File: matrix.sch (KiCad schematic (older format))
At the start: 180 parts

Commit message: Matrix work
Additional work on the switch matrix.
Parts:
- removed D? (x3): SOD-123, Diode_SMD:D_SOD-123, symbol Device:D_Small
- removed SW-M? (x2): MX_Alps-1U, MX_Alps_Hybrid:MX-1U-NoLED, symbol MX_Alps_Hybrid:MX-NoLED
- added SW-ISOEN1: MX_Alps-ISO, MX_Alps_Hybrid:MX-ISO-ReversedStabilizers, symbol MX_Alps_Hybrid:MX-NoLED
- added SW-LSHFT2: MX_Alps-1.25U, MX_Alps_Hybrid:MX-1.25U-NoLED, symbol MX_Alps_Hybrid:MX-NoLED
- added SW-STEPCAPS1: MX_Alps-1.75U, MX_Alps_Hybrid:MX-1.75U-NoLED, symbol MX_Alps_Hybrid:MX-NoLED
- SW-ANSIEN1: renamed from SW-M?; value MX_Alps-1U -> MX_Alps-2.25U; footprint MX_Alps_Hybrid:MX-1U-NoLED -> MX_Alps_Hybrid:MX-2.25U-NoLED
- SW-CAPS1, SW-RSHFT1: renamed from SW-M?; value MX_Alps-1U -> MX_Alps-1.75U; footprint MX_Alps_Hybrid:MX-1U-NoLED -> MX_Alps_Hybrid:MX-1.75U-NoLED
- SW-LSHFT1: renamed from SW-M?; footprint MX_Alps_Hybrid:MX-1U-NoLED -> MX_Alps_Hybrid:MX-2.25U-NoLED
- gave numbers to parts that had none: 42
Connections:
- wire segments 159 -> 248
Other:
- moved on the sheet: D1, D10, D11, D12, D13, D14, D15, D16, D17, D18, D19, D2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

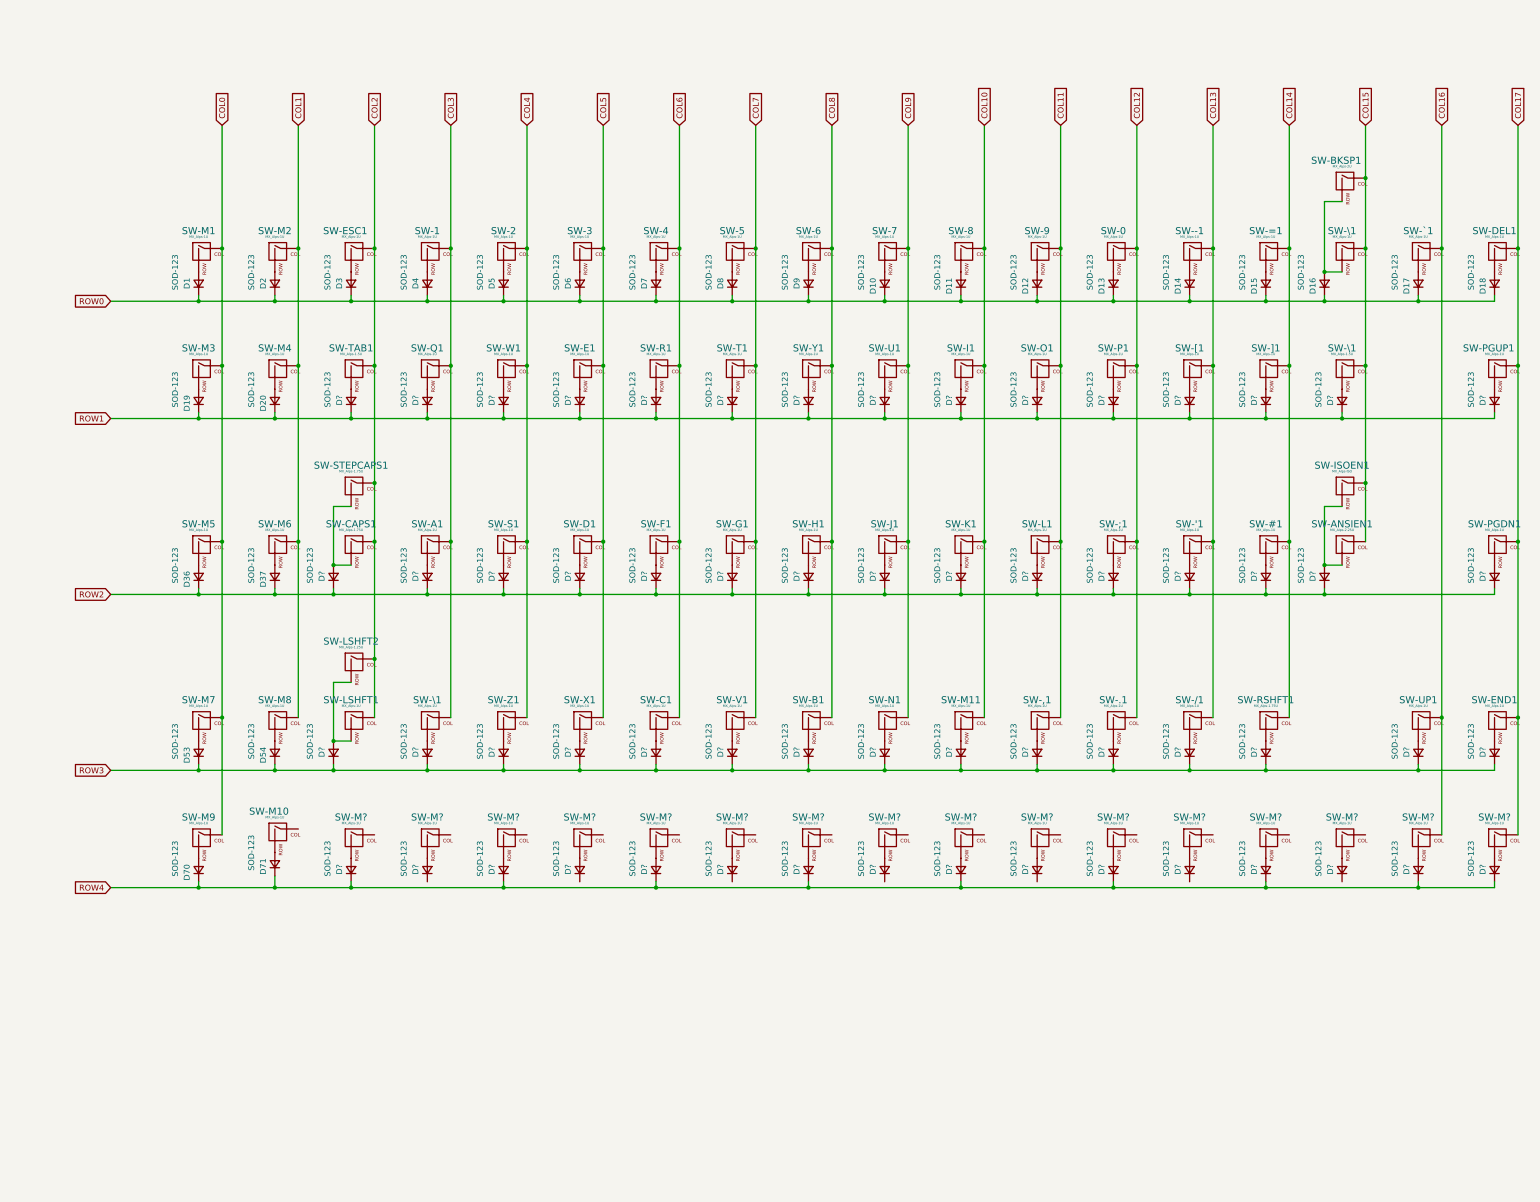
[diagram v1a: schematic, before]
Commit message: Matrix Draft complete
First draft of the switch matrix is complete.
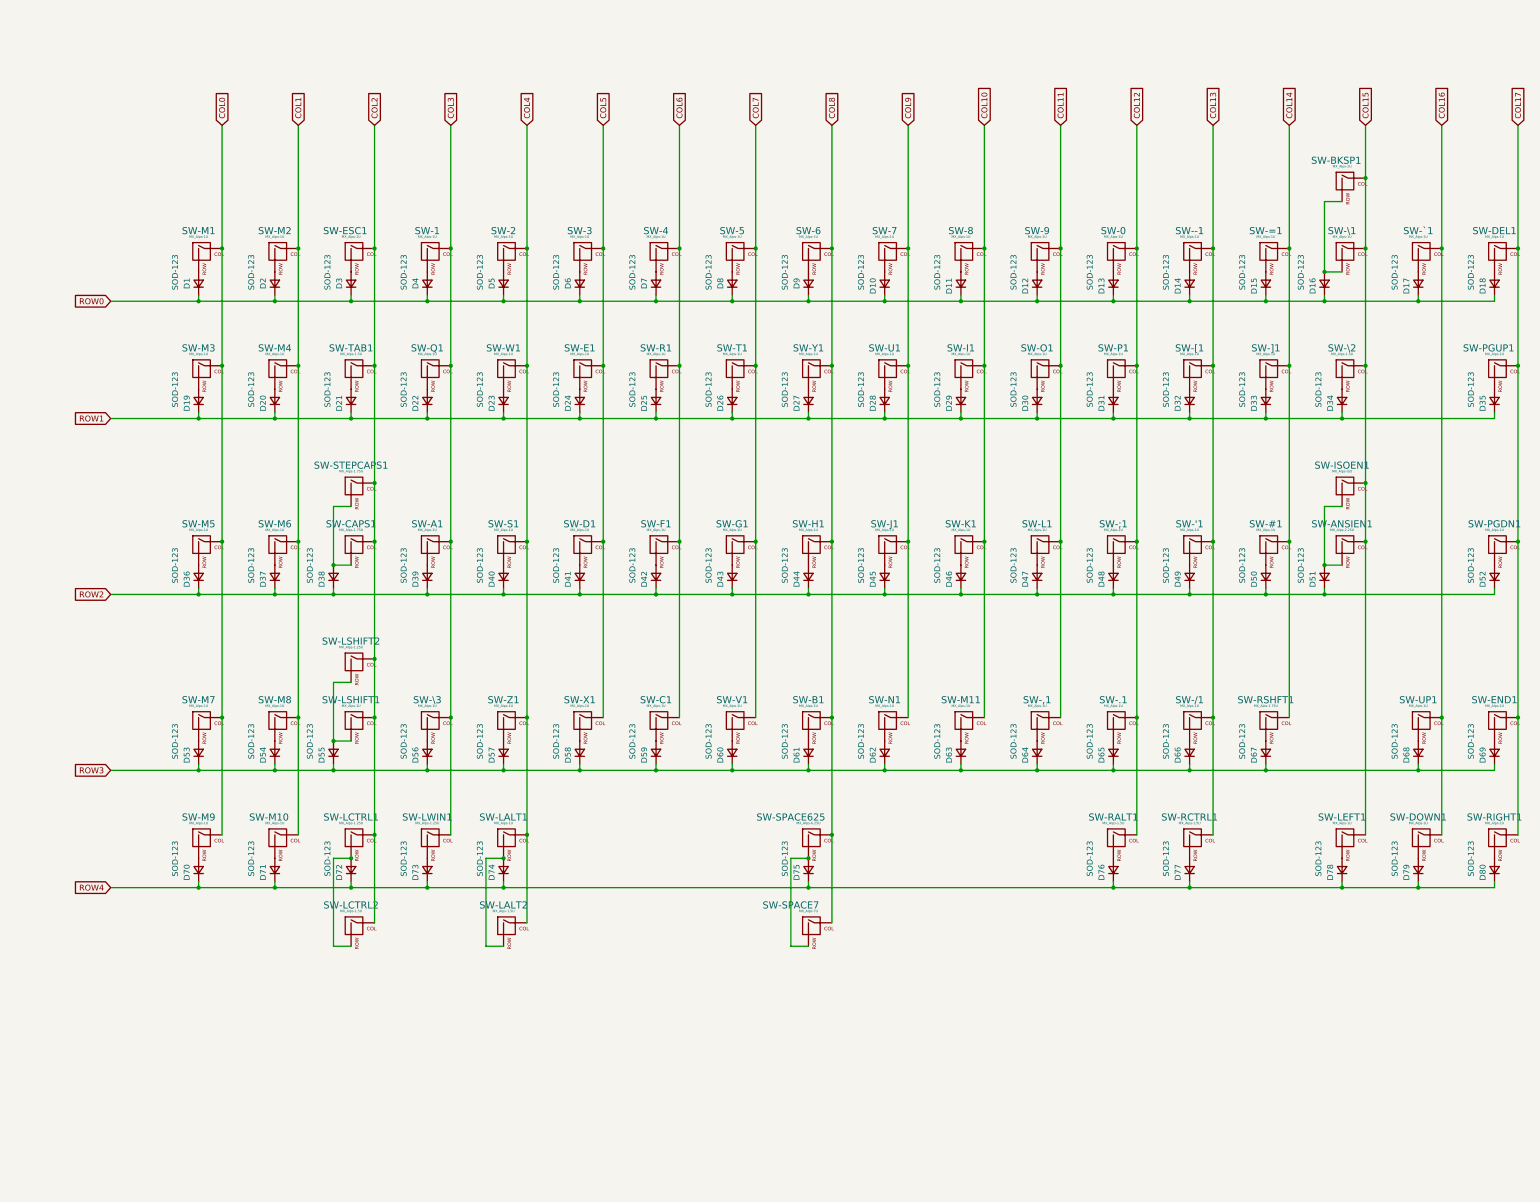
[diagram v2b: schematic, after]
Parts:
- removed D? (x7): SOD-123, Diode_SMD:D_SOD-123, symbol Device:D_Small
- removed SW-M? (x7): MX_Alps-1U, MX_Alps_Hybrid:MX-1U-NoLED, symbol MX_Alps_Hybrid:MX-NoLED
- added SW-LALT2, SW-LCTRL2: MX_Alps-1.5U, MX_Alps_Hybrid:MX-1.5U-NoLED, symbol MX_Alps_Hybrid:MX-NoLED
- added SW-SPACE7: MX_Alps-7U, MX_Alps_Hybrid:MX-7U-ReversedStabilizers-NoLED, symbol MX_Alps_Hybrid:MX-NoLED
- SW-LCTRL1, SW-LWIN1: renamed from SW-M?; value MX_Alps-1U -> MX_Alps-1.25U; footprint MX_Alps_Hybrid:MX-1U-NoLED -> MX_Alps_Hybrid:MX-1.25U-NoLED
- SW-RALT1, SW-RCTRL1: renamed from SW-M?; value MX_Alps-1U -> MX_Alps-1.5U; footprint MX_Alps_Hybrid:MX-1U-NoLED -> MX_Alps_Hybrid:MX-1.5U-NoLED
- SW-SPACE625: renamed from SW-M?; value MX_Alps-1U -> MX_Alps-6.25U; footprint MX_Alps_Hybrid:MX-1U-NoLED -> MX_Alps_Hybrid:MX-6.25U-ReversedStabilizers-NoLED
- gave numbers to parts that had none: 58
- renumbered SW-LSHFT1 to SW-LSHIFT1, SW-LSHFT2 to SW-LSHIFT2, SW-\1 to SW-\2, SW-\1 to SW-\3
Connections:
- net COL1: now also SW-M10.1 (COL)
- net COL12: now also SW-RALT1.1 (COL)
- net COL13: now also SW-RCTRL1.1 (COL)
- net COL15: now also SW-LEFT1.1 (COL)
- net COL2: now also SW-LCTRL1.1 (COL), SW-LCTRL2.1 (COL)
- net COL3: now also SW-LWIN1.1 (COL)
- net COL4: now also SW-LALT1.1 (COL), SW-LALT2.1 (COL)
- net COL8: now also SW-SPACE625.1 (COL), SW-SPACE7.1 (COL)
- net ROW4: now also D73.1 (K), D77.1 (K), D78.1 (K)
- net at D72.2 (A), SW-LCTRL1.2 (ROW): now also SW-LCTRL2.2 (ROW)
- net at D74.2 (A), SW-LALT1.2 (ROW): now also SW-LALT2.2 (ROW)
- net at D75.2 (A), SW-SPACE625.2 (ROW): now also SW-SPACE7.2 (ROW)
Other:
- moved on the sheet: D71, SW-M10

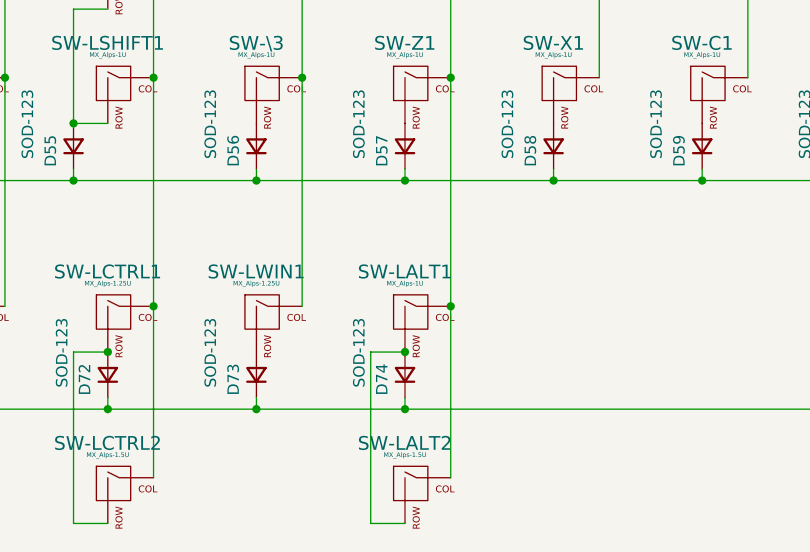
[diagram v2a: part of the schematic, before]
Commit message: PCB layout started
The beginning of the PCB layout - switch positions and two rows of diodes.
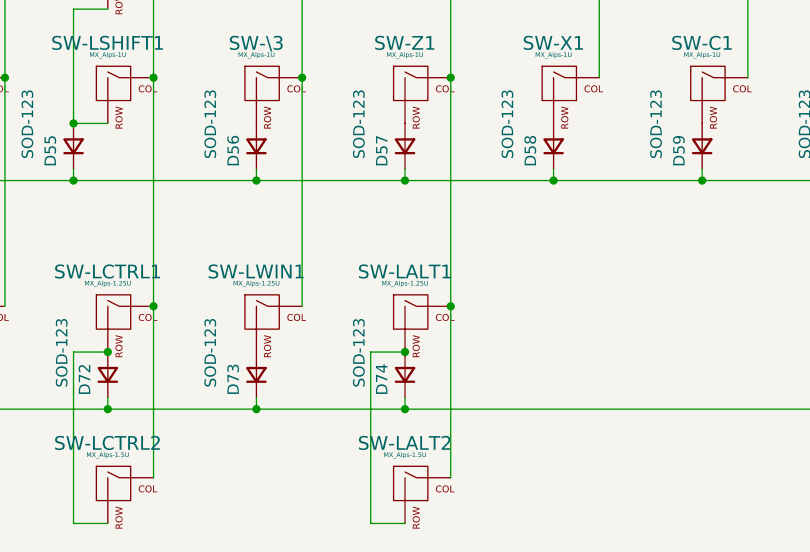
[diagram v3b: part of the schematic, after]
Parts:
- SW-LALT1: value MX_Alps-1U -> MX_Alps-1.25U; footprint MX_Alps_Hybrid:MX-1U-NoLED -> MX_Alps_Hybrid:MX-1.25U-NoLED
- SW-STEPCAPS1: footprint MX_Alps_Hybrid:MX-1.75U-NoLED -> MX_Alps_Hybrid:MX-1.25U-NoLED
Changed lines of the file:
@@
 P 5150 7850
 F 0 "SW-LALT1" H 5100 8050 60  0000 C CNN
-F 1 "MX_Alps-1U" H 5100 8000 20  0000 C CNN
-F 2 "MX_Alps_Hybrid:MX-1U-NoLED" H 4525 7825 60  0001 C CNN
+F 1 "MX_Alps-1.25U" H 5100 8000 20  0000 C CNN
+F 2 "MX_Alps_Hybrid:MX-1.25U-NoLED" H 4525 7825 60  0001 C CNN
 F 3 "" H 4525 7825 60  0001 C CNN
 	1    5150 7850
@@
 F 0 "SW-STEPCAPS1" H 3800 5050 60  0000 C CNN
 F 1 "MX_Alps-1.75U" H 3800 5000 20  0000 C CNN
-F 2 "MX_Alps_Hybrid:MX-1.75U-NoLED" H 3225 4825 60  0001 C CNN
+F 2 "MX_Alps_Hybrid:MX-1.25U-NoLED" H 3225 4825 60  0001 C CNN
 F 3 "" H 3225 4825 60  0001 C CNN
 	1    3850 4850

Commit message: Footprint changes
Changed all of the MX+Alps footprints to Alps only. Also added MX Stabilizer footprints.
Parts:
- added SW-3800CAPS1: MX_Alps-1.75U, Alps_Only:ALPS-1.5U, symbol MX_Alps_Hybrid:MX-NoLED
- added Stab-225U1, Stab-225U2: Stab-2.25U, MX_Alps_Hybrid:MX-2.25U-Stab-Only, symbol Connector_Generic:Conn_01x01
- added Stab-2U1: Stab-2U, MX_Alps_Hybrid:MX-2U-Stab-Only, symbol Connector_Generic:Conn_01x01
- added Stab-625U1: Stab-6.25U, MX_Alps_Hybrid:MX-6.25U-Stab-Only-Reversed, symbol Connector_Generic:Conn_01x01
- added Stab-7U1: Stab-7U, MX_Alps_Hybrid:MX-7U-Stab-Only-Reversed, symbol Connector_Generic:Conn_01x01
- SW-#1, SW-'1, SW-,1, SW--1, SW-.1, SW-/1, SW-0, SW-1, SW-2, SW-3, SW-4, SW-5, SW-6, SW-7, SW-8, SW-9, SW-;1, SW-=1, SW-A1, SW-B1, SW-C1, SW-D1, SW-DEL1, SW-DOWN1, SW-E1, SW-END1, SW-ESC1, SW-F1, SW-G1, SW-H1, SW-I1, SW-J1, SW-K1, SW-L1, SW-LEFT1, SW-M1, SW-M10, SW-M11, SW-M2, SW-M3, SW-M4, SW-M5, SW-M6, SW-M7, SW-M8, SW-M9, SW-N1, SW-O1, SW-P1, SW-PGDN1, SW-PGUP1, SW-Q1, SW-R1, SW-RIGHT1, SW-S1, SW-T1, SW-U1, SW-UP1, SW-V1, SW-W1, SW-X1, SW-Y1, SW-Z1, SW-[1, SW-\1, SW-\3, SW-]1, SW-`1: footprint MX_Alps_Hybrid:MX-1U-NoLED -> Alps_Only:ALPS-1U
- SW-ANSIEN1, SW-LSHIFT1: footprint MX_Alps_Hybrid:MX-2.25U-NoLED -> Alps_Only:ALPS-2.25U
- SW-BKSP1: footprint MX_Alps_Hybrid:MX-2U-NoLED -> Alps_Only:ALPS-2U
- SW-CAPS1, SW-RSHFT1: footprint MX_Alps_Hybrid:MX-1.75U-NoLED -> Alps_Only:ALPS-1.75U
- SW-ISOEN1: footprint MX_Alps_Hybrid:MX-ISO-ReversedStabilizers -> Alps_Only:ALPS-ISO-FLIPPED
- SW-LALT1, SW-LCTRL1, SW-LSHIFT2, SW-LWIN1, SW-STEPCAPS1: footprint MX_Alps_Hybrid:MX-1.25U-NoLED -> Alps_Only:ALPS-1.25U
- SW-LALT2, SW-LCTRL2, SW-RALT1, SW-RCTRL1, SW-TAB1, SW-\2: footprint MX_Alps_Hybrid:MX-1.5U-NoLED -> Alps_Only:ALPS-1.5U
- SW-SPACE625: footprint MX_Alps_Hybrid:MX-6.25U-ReversedStabilizers-NoLED -> Alps_Only:ALPS-6.25U
- SW-SPACE7: footprint MX_Alps_Hybrid:MX-7U-ReversedStabilizers-NoLED -> Alps_Only:ALPS-7U
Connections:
- net COL2: now also SW-3800CAPS1.1 (COL)
- net at D38.2 (A), SW-CAPS1.2 (ROW), SW-STEPCAPS1.2 (ROW): now also SW-3800CAPS1.2 (ROW)
- no-connect marks 0 -> 5
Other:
- moved on the sheet: SW-STEPCAPS1

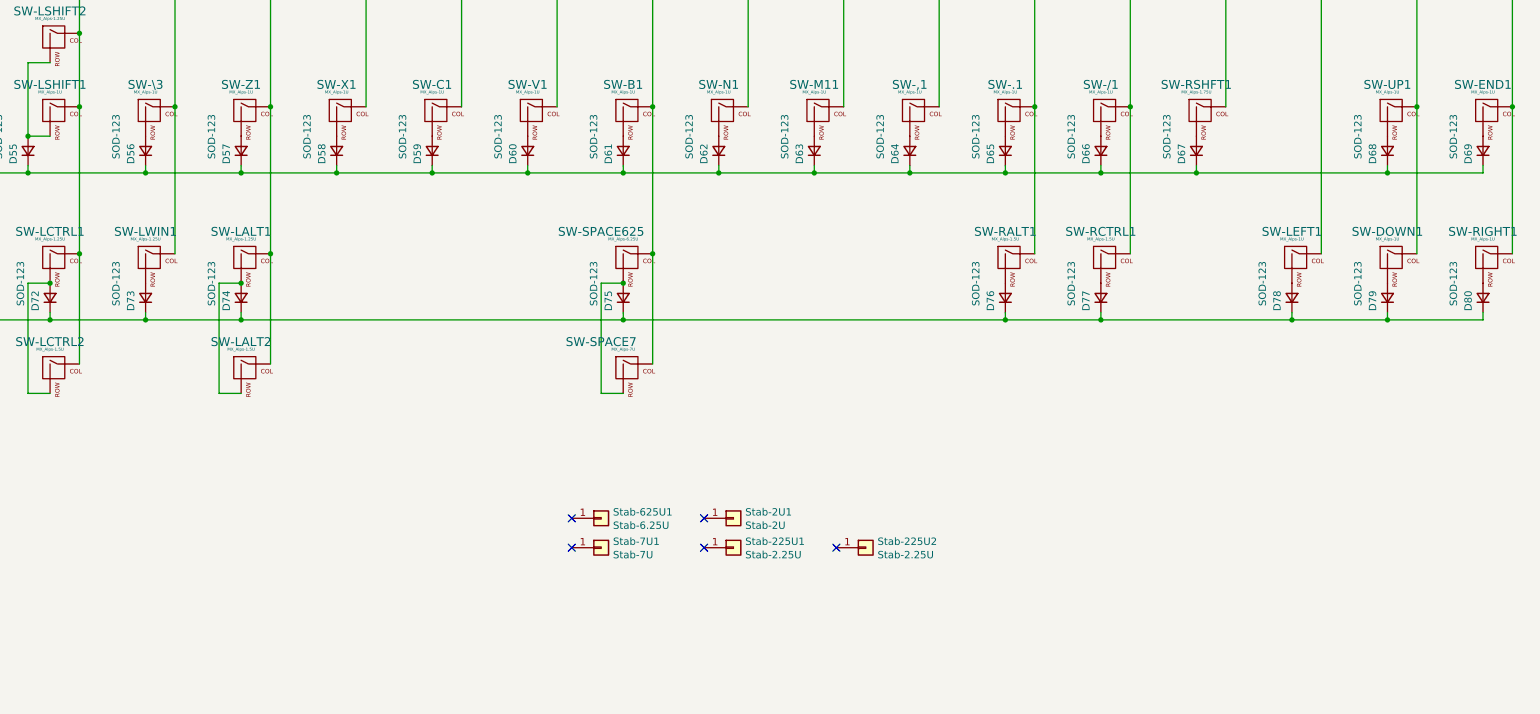
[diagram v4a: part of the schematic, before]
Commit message: Initial routing and additional switch footprints
More bottom row option support (6U, split spacebar), and the start of some column and row routing.
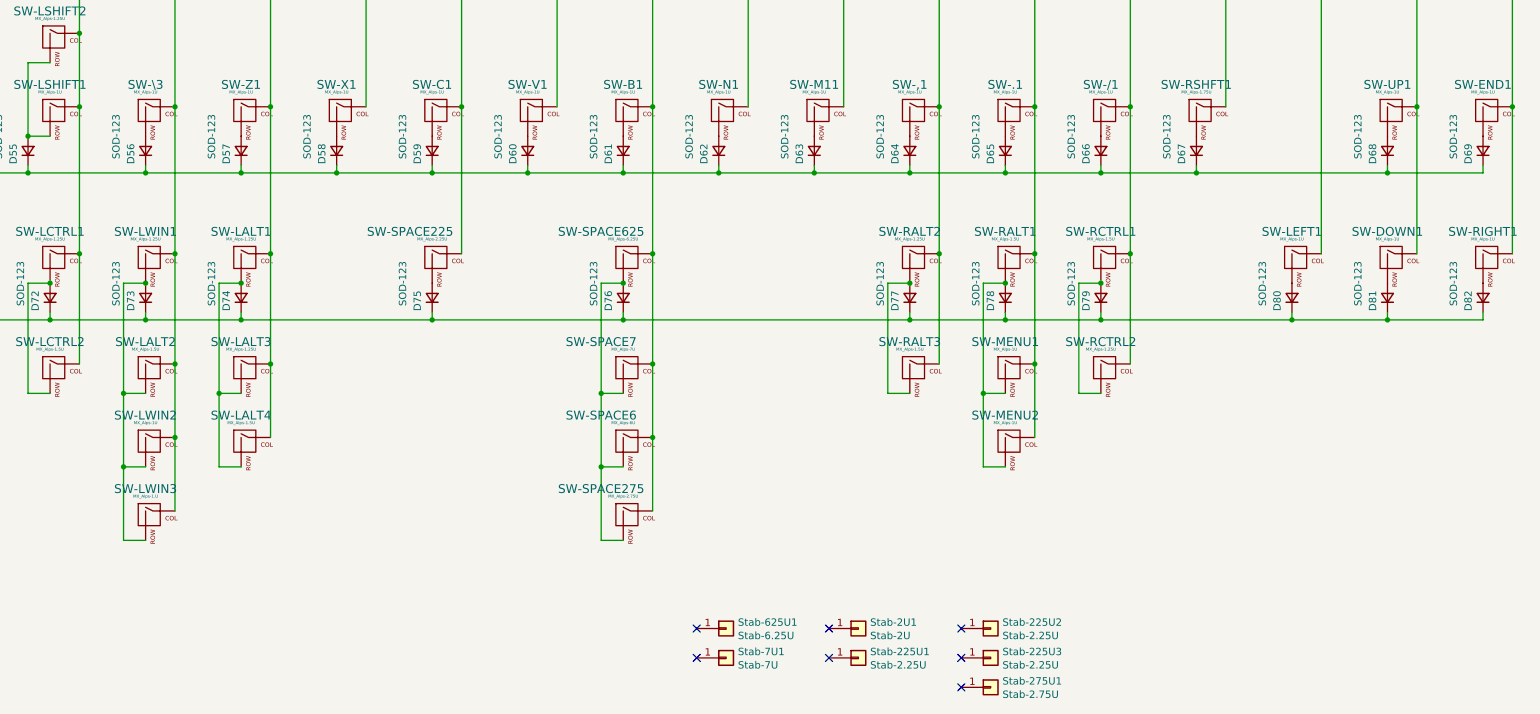
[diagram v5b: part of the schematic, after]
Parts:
- added D75, D77: SOD-123, Diode_SMD:D_SOD-123, symbol Device:D_Small
- added SW-LALT3, SW-RALT2, SW-RCTRL2: MX_Alps-1.25U, Alps_Only:ALPS-1.25U, symbol MX_Alps_Hybrid:MX-NoLED
- added SW-LALT4, SW-RALT3: MX_Alps-1.5U, Alps_Only:ALPS-1.5U, symbol MX_Alps_Hybrid:MX-NoLED
- added SW-LWIN2, SW-MENU1, SW-MENU2: MX_Alps-1U, Alps_Only:ALPS-1U, symbol MX_Alps_Hybrid:MX-NoLED
- added SW-LWIN3: MX_Alps-1.U, Alps_Only:ALPS-1U, symbol MX_Alps_Hybrid:MX-NoLED
- added SW-SPACE225: MX_Alps-2.25U, Alps_Only:ALPS-2.25U, symbol MX_Alps_Hybrid:MX-NoLED
- added SW-SPACE275: MX_Alps-2.75U, Alps_Only:ALPS-2.75U, symbol MX_Alps_Hybrid:MX-NoLED
- added SW-SPACE6: MX_Alps-6U, MX_Alps_Hybrid:MX-6U-Centered-ReversedStabilizers-NoLED, symbol MX_Alps_Hybrid:MX-NoLED
- added Stab-225U2: Stab-2.25U, MX_Alps_Hybrid:MX-2.25U-Stab-Only, symbol Connector_Generic:Conn_01x01
- added Stab-275U1: Stab-2.75U, MX_Alps_Hybrid:MX-2.75U-Stab-Only, symbol Connector_Generic:Conn_01x01
- renumbered D75 to D76, D76 to D78, D77 to D79, D78 to D80, D79 to D81, D80 to D82, Stab-225U2 to Stab-225U3
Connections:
- net COL11: now also SW-RALT2.1 (COL), SW-RALT3.1 (COL)
- net COL12: now also SW-MENU1.1 (COL), SW-MENU2.1 (COL)
- net COL13: now also SW-RCTRL2.1 (COL)
- net COL3: now also SW-LALT2.1 (COL), SW-LWIN2.1 (COL), SW-LWIN3.1 (COL)
- net COL4: now also SW-LALT3.1 (COL), SW-LALT4.1 (COL); no longer SW-LALT2.1 (COL)
- net COL6: now also SW-SPACE225.1 (COL)
- net COL8: now also SW-SPACE275.1 (COL), SW-SPACE6.1 (COL)
- net ROW4: now also D75.1 (K), D77.1 (K)
- net at D76.2 (A), SW-SPACE625.2 (ROW), SW-SPACE7.2 (ROW): now also SW-SPACE275.2 (ROW), SW-SPACE6.2 (ROW)
- net at D73.2 (A), SW-LWIN1.2 (ROW): now also SW-LALT2.2 (ROW), SW-LWIN2.2 (ROW), SW-LWIN3.2 (ROW)
- net at D74.2 (A), SW-LALT1.2 (ROW): now also SW-LALT3.2 (ROW), SW-LALT4.2 (ROW); no longer SW-LALT2.2 (ROW)
- net at D78.2 (A), SW-RALT1.2 (ROW): now also SW-MENU1.2 (ROW), SW-MENU2.2 (ROW)
- net at D79.2 (A), SW-RCTRL1.2 (ROW): now also SW-RCTRL2.2 (ROW)
- new net: D77.2 (A), SW-RALT2.2 (ROW), SW-RALT3.2 (ROW)
- new net: D75.2 (A), SW-SPACE225.2 (ROW)
- no-connect marks 5 -> 7
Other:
- moved on the sheet: SW-LALT2, Stab-225U1, Stab-225U3, Stab-2U1, Stab-625U1, Stab-7U1

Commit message: Generate Gerber, BOM, and POS files
Generated production files, including Gerbers, BOM for JLCPCB, and positioning files (specific to JLCPCB).
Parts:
- D1, D10, D11, D12, D13, D14, D15, D16, D17, D18, D19, D2, D20, D21, D22, D23, D24, D25, D26, D27, D28, D29, D3, D30, D31, D32, D33, D34, D35, D36, D37, D38, D39, D4, D40, D41, D42, D43, D44, D45, D46, D47, D48, D49, D5, D50, D51, D52, D53, D54, D55, D56, D57, D58, D59, D6, D60, D61, D62, D63, D64, D65, D66, D67, D68, D69, D7, D70, D71, D72, D73, D74, D75, D76, D77, D78, D79, D8, D80, D81, D82, D9: LCSC (none) -> C81598
